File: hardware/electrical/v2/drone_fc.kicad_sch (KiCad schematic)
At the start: 29 parts, among them J1 ESC_4IN1_JST_SH, J3 Cortex_SWD_10P, U1 MDBT53-P1M, U2 ICM-42688-P, U3 LMR50410_Buck, U4 TLV75533PDBVR

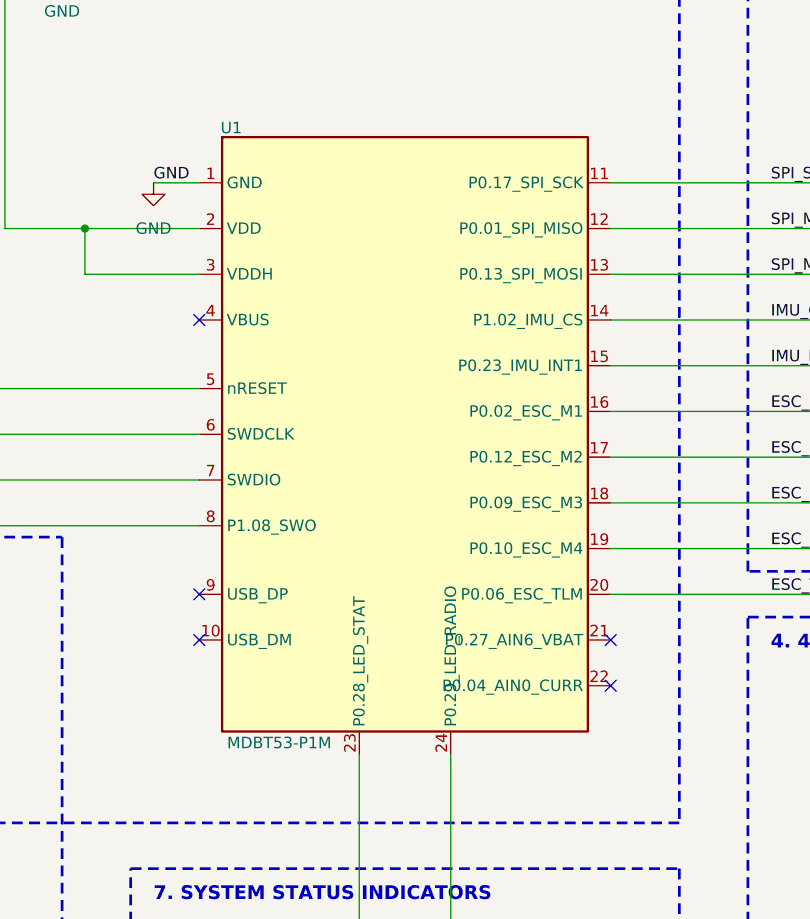
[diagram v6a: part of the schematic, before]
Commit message: mdbt53: fix symbol pin numbers to match real module pads
The MDBT53_P1M symbol's pin numbers were assigned by schematic
drawing order (1..24), not the real Raytac pad numbers used by the
converted footprint. KiCad matches symbol pin number to footprint
pad name, so every signal pin except GND was wired to the wrong
physical pad - VDD would have landed on the SWCLK debug pad,
nRESET on an analog input, SPI_MISO nowhere near P0.01, etc.

Verified against the full pin table in doc/hardware/[nRF5340]
MDBT53-1M & MDBT53-P1M_Ver.E spec.pdf and remapped every pin to its
real pad number. While remapping, reassigned the freely-choosable
GPIO signals to two contiguous pad runs for cleaner layout:
  - IMU SPI bus + INT1 -> pads 15-19 (left edge)
  - ESC M1-4 + telemetry -> pads 25-29 (bottom edge)
  - Status/radio LEDs -> pads 64-65 (top edge, clear of both buses)

Confirmed against Raytac's LDO-mode reference circuit (section 8.1)
that DCC/DCCH/DCCD/DECD/DECR (the DC-DC regulator pins) are meant
to be no-connect when running in LDO mode, so no schematic pins are
needed for them - to be marked NC in the PCB editor during layout.

ERC: 0 errors, 0 warnings.
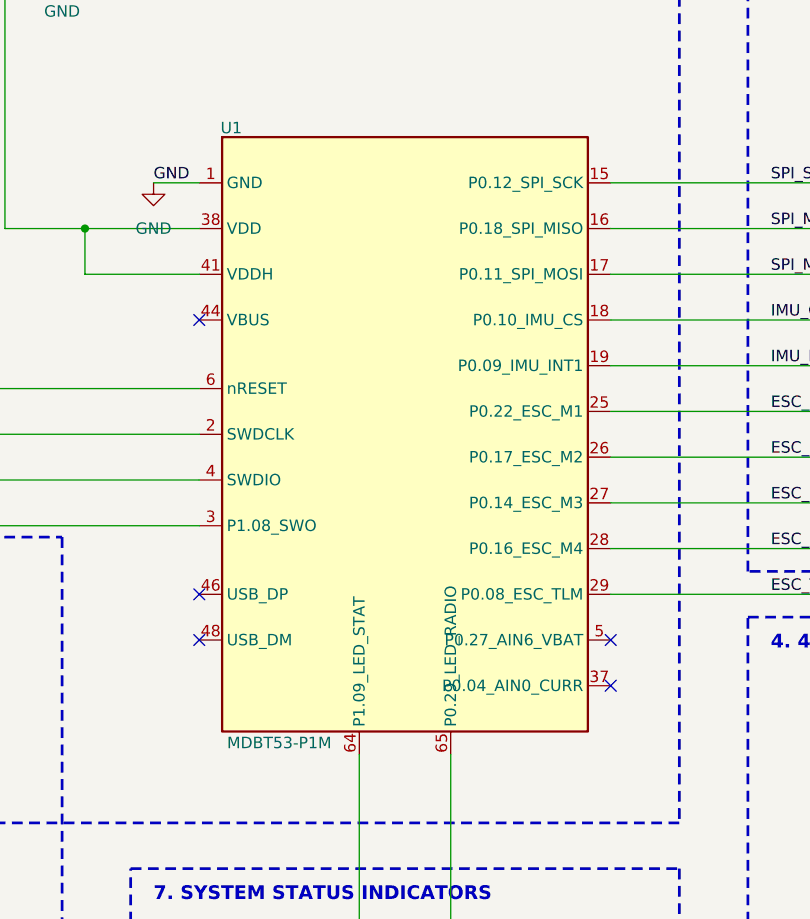
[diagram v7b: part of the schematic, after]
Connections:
- net +3V3: now also U1.38 (VDD), U1.41 (VDDH); no longer U1.2 (VDD), U1.3 (VDDH)
- net ESC_M1: now also U1.25 (P0.22_ESC_M1); no longer U1.16 (P0.02_ESC_M1)
- net ESC_M2: now also U1.26 (P0.17_ESC_M2); no longer U1.17 (P0.12_ESC_M2)
- net ESC_M3: now also U1.27 (P0.14_ESC_M3); no longer U1.18 (P0.09_ESC_M3)
- net ESC_M4: now also U1.28 (P0.16_ESC_M4); no longer U1.19 (P0.10_ESC_M4)
- net ESC_TLM: now also U1.29 (P0.08_ESC_TLM); no longer U1.20 (P0.06_ESC_TLM)
- net IMU_CS: now also U1.18 (P0.10_IMU_CS); no longer U1.14 (P1.02_IMU_CS)
- net IMU_INT1: now also U1.19 (P0.09_IMU_INT1); no longer U1.15 (P0.23_IMU_INT1)
- net SPI_MISO: now also U1.16 (P0.18_SPI_MISO); no longer U1.12 (P0.01_SPI_MISO)
- net SPI_MOSI: now also U1.17 (P0.11_SPI_MOSI); no longer U1.13 (P0.13_SPI_MOSI)
- net SPI_SCK: now also U1.15 (P0.12_SPI_SCK); no longer U1.11 (P0.17_SPI_SCK)
- net SWDCLK: now also U1.2 (SWDCLK); no longer U1.6 (SWDCLK)
- net SWDIO: now also U1.4 (SWDIO); no longer U1.7 (SWDIO)
- net SWO: now also U1.3 (P1.08_SWO); no longer U1.8 (P1.08_SWO)
- net nRESET: now also U1.6 (nRESET); no longer U1.5 (nRESET)
- net at D1.1 (A): now also U1.64 (P1.09_LED_STAT); no longer U1.23 (P0.28_LED_STAT)
- net at D2.1 (A): now also U1.65 (P0.29_LED_RADIO); no longer U1.24 (P0.29_LED_RADIO)

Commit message: schematic: re-annotate reference designators, close R1/R2/R5/R6 gap
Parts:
- C1: renamed from C2; value 10uF_50V -> 10uF; footprint Capacitor_SMD:C_0402_1005Metric -> Capacitor_SMD:C_1210_3225Metric
- C5: renamed from C3; value 22uF_10V -> 22uF; footprint Capacitor_SMD:C_0402_1005Metric -> Capacitor_SMD:C_0805_2012Metric
- C6: renamed from C4; footprint Capacitor_SMD:C_0402_1005Metric -> Capacitor_SMD:C_0603_1608Metric
- R3, R4: value 1k_1% -> 1k
- renumbered C6 to C10, C11 to C2, C10 to C3, C1 to C4, C12 to C7, C13 to C8, C5 to C9, J3 to J1, J1 to J2, R11 to R1, R12 to R2, R7 to R5, R8 to R6, R9 to R7, R13 to R8, R10 to R9, U4 to U1, U3 to U2, U1 to U3, U2 to U4
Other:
- moved on the sheet: D1, D2, R3, R4
